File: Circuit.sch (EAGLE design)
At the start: 3 parts

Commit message: Added all the sensor components
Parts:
- added ITG1, ITG2, ITG3: ITG-3050, Gyros:ITG-3050
- added MPU1: MPU-3300, Gyros:MPU-3300
- added U1, U2: MAG3110, Gyros:MAG3110
- added U10, U7, U8, U9: MMA8452Q, SparkFun:MMA8452Q
- added U3, U4, U5, U6: L3G4200D, Gyros:L3G4200D
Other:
- moved on the sheet: ITG, MPU, U$1
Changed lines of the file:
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@@
 <part name="U$1" library="RaspberryPi" deviceset="RASPBERRY-PI_REV2" device=""/>
 <part name="ITG" library="Gyros" deviceset="ITG-3050" device=""/>
+<part name="MPU1" library="Gyros" deviceset="MPU-3300" device=""/>
+<part name="ITG1" library="Gyros" deviceset="ITG-3050" device=""/>
+<part name="ITG2" library="Gyros" deviceset="ITG-3050" device=""/>
+<part name="ITG3" library="Gyros" deviceset="ITG-3050" device=""/>
+<part name="U1" library="Gyros" deviceset="MAG3110" device=""/>
+<part name="U2" library="Gyros" deviceset="MAG3110" device=""/>
+<part name="U3" library="Gyros" deviceset="L3G4200D" device=""/>
+<part name="U4" library="Gyros" deviceset="L3G4200D" device=""/>
+<part name="U5" library="Gyros" deviceset="L3G4200D" device=""/>
+<part name="U6" library="Gyros" deviceset="L3G4200D" device=""/>
+<part name="U7" library="SparkFun" deviceset="MMA8452Q" device=""/>
+<part name="U8" library="SparkFun" deviceset="MMA8452Q" device=""/>
+<part name="U9" library="SparkFun" deviceset="MMA8452Q" device=""/>
+<part name="U10" library="SparkFun" deviceset="MMA8452Q" device=""/>
 </parts>
 <sheets>
@@
 </plain>
 <instances>
-<instance part="MPU" gate="G$1" x="124.06" y="71.68"/>
-<instance part="U$1" gate="G$1" x="181.58" y="-34.48"/>
-<instance part="ITG" gate="G$1" x="246.38" y="71.12"/>
+<instance part="MPU" gate="G$1" x="103.74" y="147.88"/>
+<instance part="U$1" gate="G$1" x="415.26" y="-31.94"/>
+<instance part="ITG" gate="G$1" x="246.38" y="86.36"/>
+<instance part="MPU1" gate="G$1" x="245.98" y="147.88"/>
+<instance part="ITG1" gate="G$1" x="104.14" y="86.36"/>
+<instance part="ITG2" gate="G$1" x="104.14" y="43.18"/>
+<instance part="ITG3" gate="G$1" x="246.38" y="43.18"/>
+<instance part="U1" gate="G$1" x="104.14" y="-111.76"/>
+<instance part="U2" gate="G$1" x="246.38" y="-111.76"/>
+<instance part="U3" gate="G$1" x="246.38" y="-20.32"/>
+<instance part="U4" gate="G$1" x="104.14" y="-20.32"/>
+<instance part="U5" gate="G$1" x="104.14" y="-66.04"/>
+<instance part="U6" gate="G$1" x="246.38" y="-66.04"/>
+<instance part="U7" gate="G$1" x="383.54" y="134.62"/>
+<instance part="U8" gate="G$1" x="454.66" y="134.62"/>
+<instance part="U9" gate="G$1" x="383.54" y="91.44"/>
+<instance part="U10" gate="G$1" x="454.66" y="91.44"/>
 </instances>
 <busses>

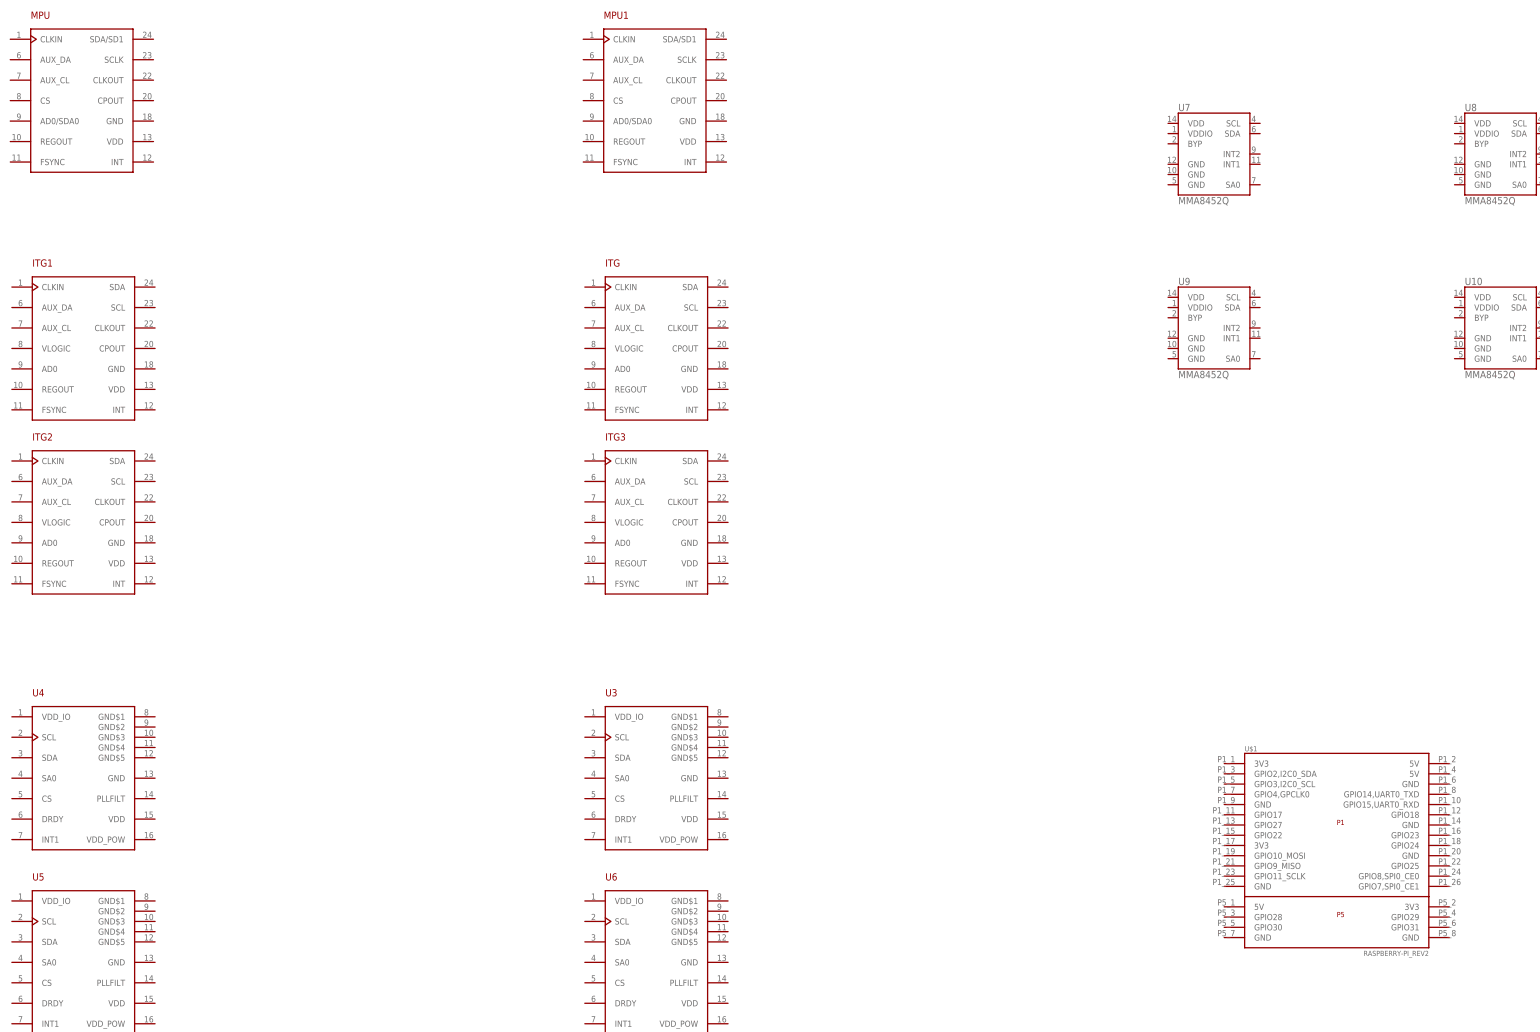
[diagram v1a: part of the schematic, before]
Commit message: Adds first routes
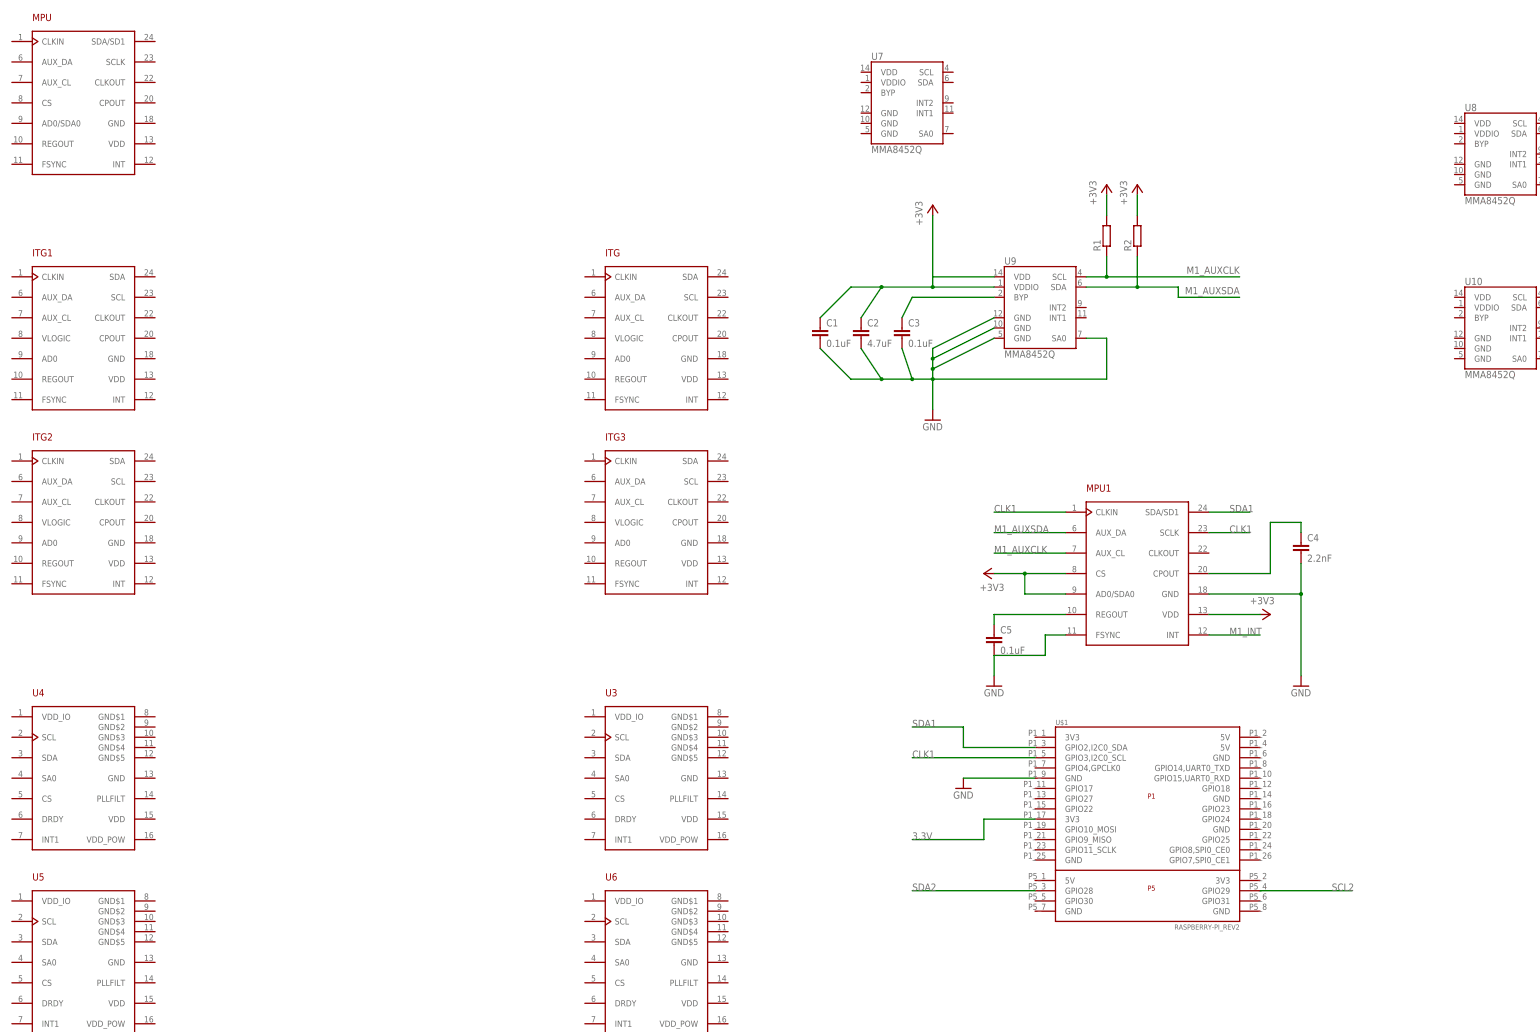
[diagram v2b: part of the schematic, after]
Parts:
- added C1, C3, C5: 0.1uF, SparkFun:CAP0402-CAP
- added C2: 4.7uF, SparkFun:CAP0402-CAP
- added C4: 2.2nF, SparkFun:CAP0402-CAP
- added R1, R2: (no value), resistor:R-EU_0207/10
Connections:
- new net +3V3: C1.1, C2.1, MPU1.AD0/SDA0, MPU1.CS, MPU1.VDD, R1.2, R2.2, U9.VDD, U9.VDDIO
- new net 3.3V: U$1.3V3@17
- new net CLK1: MPU1.CLKIN, MPU1.SCLK, U$1.GPIO3,I2C0_SCL
- new net GND: C1.2, C2.2, C3.2, C4.2, C5.2, MPU1.FSYNC, MPU1.GND, U$1.GND@9, U9.GND@0, U9.GND@1, U9.GND@2, U9.SA0
- new net M1_AUXCLK: MPU1.AUX_CL, R1.1, U9.SCL
- new net M1_AUXSDA: MPU1.AUX_DA, R2.1, U9.SDA
- new net M1_INT: MPU1.INT
- new net N$1: C4.1, MPU1.CPOUT
- new net N$2: C5.1, MPU1.REGOUT
- new net N$3: C3.1, U9.BYP
- new net SCL2: U$1.GPIO29
- new net SDA1: MPU1.SDA/SD1, U$1.GPIO2,I2C0_SDA
- new net SDA2: U$1.GPIO28
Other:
- moved on the sheet: ITG, ITG1, MPU, MPU1, U$1, U7, U9

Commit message: Added 4 itg setups
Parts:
- removed ITG: ITG-3050, Gyros:ITG-3050
- removed MPU: MPU-3300, Gyros:MPU-3300
- added C10, C11, C13, C14, C16, C18, C20, C21, C23, C25, C27, C28, C30, C32, C34, C35, C37, C6, C8: 0.1uF, SparkFun:CAP0402-CAP
- added C12, C19, C26, C33, C7: 4.7uF, SparkFun:CAP0402-CAP
- added C15, C22, C29, C36, C9: 2.2nF, SparkFun:CAP0402-CAP
- added C17, C24, C31, C38: 10nF, SparkFun:CAP0402-CAP
- added ITG4: ITG-3050, Gyros:ITG-3050
- added MPU2: MPU-3300, Gyros:MPU-3300
- added R10, R11, R12, R3, R4, R5, R6, R7, R8, R9: 10K, resistor:R-EU_0207/10
- added U11, U12: MMA8452Q, SparkFun:MMA8452Q
- R1, R2: value (none) -> 10K
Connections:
- removed net 3.3V: U$1.3V3@17
- removed net M1_INT: MPU1.INT
- new net CLK2: ITG2.SCL, ITG4.SCL, MPU2.SCLK
- new net I1_AUXCLK: ITG1.AUX_CL, U7.SCL
- new net I1_AUXSDA: ITG1.AUX_DA, U7.SDA
- new net I1_INT: ITG1.INT
- new net I2_AUXCLK: ITG2.AUX_CL, U8.SCL
- new net I2_AUXSDA: ITG2.AUX_DA, U8.SDA
- new net I2_INT: ITG2.INT
- new net I3_AUXCLK: ITG3.AUX_CL, U10.SCL
- new net I3_AUXSDA: ITG3.AUX_DA, U10.SDA
- new net I3_INT: ITG3.INT
- new net I4_AUXCLK: ITG4.AUX_CL, U12.SCL
- new net I4_AUXSDA: ITG4.AUX_DA, U12.SDA
- new net I4_INT: ITG4.INT
- new net M2_AUXCLK: MPU2.AUX_CL, R3.1, U11.SCL
- new net M2_AUXSDA: MPU2.AUX_DA, R4.1, U11.SDA
- new net M2_INT: MPU1.INT, MPU2.INT
- new net N$11: R5.1
- new net N$12: R6.1
- new net N$13: C14.1, ITG1.REGOUT
- new net N$14: C15.1, ITG1.CPOUT
- new net N$15: C20.1, U8.BYP
- new net N$18: R7.1
- new net N$19: R8.1
- new net N$20: C21.1, ITG2.REGOUT
- new net N$21: C22.1, ITG2.CPOUT
- new net N$23: C27.1, U10.BYP
- new net N$25: R9.1
- new net N$26: R10.1
- new net N$27: C28.1, ITG3.REGOUT
- new net N$28: C29.1, ITG3.CPOUT
- new net N$30: C34.1, U12.BYP
- new net N$32: R11.1
- new net N$33: R12.1
- new net N$34: C35.1, ITG4.REGOUT
- new net N$35: C36.1, ITG4.CPOUT
- new net N$5: C8.1, U11.BYP
- new net N$6: C9.1, MPU2.CPOUT
- new net N$7: C10.1, MPU2.REGOUT
- new net N$9: C13.1, U7.BYP
- net +3V3: now also C11.1, C12.1, C15.2, C16.1, C16.2, C17.1, C18.1, C19.1, C22.2, C23.1, C23.2, C24.1, C25.1, C26.1, C29.2, C30.1, C30.2, C31.1, C32.1, C33.1, C36.2, C37.1, C37.2, C38.1, C6.1, C7.1, ITG1.GND, ITG1.VDD, ITG1.VLOGIC, ITG2.GND, ITG2.VDD, ITG2.VLOGIC, ITG3.GND, ITG3.VDD, ITG3.VLOGIC, ITG4.GND, ITG4.VDD, ITG4.VLOGIC, MPU2.CS, MPU2.VDD, R10.2, R11.2, R12.2, R3.2, R4.2, R5.2, R6.2, R7.2, R8.2, R9.2, U$1.3V3@17, U10.VDD, U10.VDDIO, U11.VDD, U11.VDDIO, U12.VDD, U12.VDDIO, U7.VDD, U7.VDDIO, U8.VDD, U8.VDDIO
- net CLK1: now also ITG1.SCL, ITG3.SCL; no longer MPU1.CLKIN
- net GND: now also C10.2, C11.2, C12.2, C13.2, C14.2, C17.2, C18.2, C19.2, C20.2, C21.2, C24.2, C25.2, C26.2, C27.2, C28.2, C31.2, C32.2, C33.2, C34.2, C35.2, C38.2, C6.2, C7.2, C8.2, C9.2, ITG1.CLKIN, ITG1.FSYNC, ITG2.CLKIN, ITG2.FSYNC, ITG3.CLKIN, ITG3.FSYNC, ITG4.CLKIN, ITG4.FSYNC, MPU1.CLKIN, MPU2.AD0/SDA0, MPU2.CLKIN, MPU2.FSYNC, MPU2.GND, U10.GND@0, U10.GND@1, U10.GND@2, U10.SA0, U11.GND@0, U11.GND@1, U11.GND@2, U11.SA0, U12.GND@0, U12.GND@1, U12.GND@2, U12.SA0, U7.GND@0, U7.GND@1, U7.GND@2, U7.SA0, U8.GND@0, U8.GND@1, U8.GND@2, U8.SA0
- net SDA1: now also ITG1.SDA, ITG3.SDA
- net SDA2: now also ITG2.SDA, ITG4.SDA, MPU2.SDA/SD1
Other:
- note added: "MPU/MMA_1"
- note added: "MPU/MMA_2"
- moved on the sheet: C1, C2, C3, C4, C5, ITG1, ITG2, ITG3, MPU1, R1, R2, U$1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

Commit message: Added L3G4 gyros
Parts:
- added C39, C43, C47, C51: 0.1uF, SparkFun:CAP0402-CAP
- added C40, C44, C48, C52: 10uF, SparkFun:CAP0402-CAP
- added C41, C45, C49, C53: 10nF, SparkFun:CAP0402-CAP
- added C42, C46, C50, C54: 470nF, SparkFun:CAP0402-CAP
- added R13, R14, R15, R16, R17, R18, R19, R20, R21, R22, R23, R24: 10K, resistor:R-EU_0207/10
- U3, U4, U5, U6: device Gyros:L3G4200D -> SparkFun:L3G4200D
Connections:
- new net N$36: C45.1, C46.1, U4.PLL
- new net N$39: C41.1, C42.1, U3.PLL
- new net N$40: C42.2, R15.2
- new net N$41: C46.2, R18.2
- new net N$45: C49.1, C50.1, U5.PLL
- new net N$46: C50.2, R21.2
- new net N$50: C53.1, C54.1, U6.PLL
- new net N$51: C54.2, R24.2
- net +3V3: now also C39.1, C40.1, C43.1, C44.1, C47.1, C48.1, C51.1, C52.1, R13.1, R14.1, R16.1, R17.1, R19.1, R20.1, R22.1, R23.1, U3.CS, U3.RSVDV@0, U3.VDD, U3.VDDIO, U4.CS, U4.RSVDV@0, U4.SDO, U4.VDD, U4.VDDIO, U5.CS, U5.RSVDV@0, U5.VDD, U5.VDDIO, U6.CS, U6.RSVDV@0, U6.SDO, U6.VDD, U6.VDDIO
- net CLK1: now also R13.2, R16.2, U3.SCL, U4.SCL
- net CLK2: now also R19.2, R22.2, U5.SCL, U6.SCL
- net GND: now also C39.2, C40.2, C41.2, C43.2, C44.2, C45.2, C47.2, C48.2, C49.2, C51.2, C52.2, C53.2, R15.1, R18.1, R21.1, R24.1, U3.GND, U3.RSDVG@3, U3.RSVDG@0, U3.RSVDG@1, U3.RSVDG@2, U3.RSVDG@4, U3.SDO, U4.GND, U4.RSDVG@3, U4.RSVDG@0, U4.RSVDG@1, U4.RSVDG@2, U4.RSVDG@4, U5.GND, U5.RSDVG@3, U5.RSVDG@0, U5.RSVDG@1, U5.RSVDG@2, U5.RSVDG@4, U5.SDO, U6.GND, U6.RSDVG@3, U6.RSVDG@0, U6.RSVDG@1, U6.RSVDG@2, U6.RSVDG@4
- net SDA1: now also R14.2, R17.2, U3.SDA/SDI, U4.SDA/SDI
- net SDA2: now also R20.2, R23.2, U5.SDA/SDI, U6.SDA/SDI
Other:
- moved on the sheet: U$1, U1, U2

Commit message: Added mags and box labels
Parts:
- added C55, C56, C57, C58: 0.1uF, SparkFun:CAP0402-CAP
- added R25, R26, R27, R28: 4.7K, resistor:R-EU_0207/10
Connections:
- new net MAG1_INT: U1.INT1
- new net MAG2_INT: U2.INT1
- new net N$38: C55.1, U2.CAP-A
- new net N$49: C56.1, U2.CAP-R
- new net N$52: C57.1, U1.CAP-A
- new net N$53: C58.1, U1.CAP-R
- net +3V3: now also R25.2, R26.2, R27.2, R28.2, U1.VDD, U1.VDDIO, U2.VDD, U2.VDDIO
- net CLK1: now also R28.1, U1.SCL
- net CLK2: now also R26.1, U2.SCL
- net GND: now also C55.2, C56.2, C57.2, C58.2, U1.GND@10, U1.GND@5, U2.GND@10, U2.GND@5
- net SDA1: now also R27.1, U1.SDA
- net SDA2: now also R25.1, U2.SDA
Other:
- moved on the sheet: U1, U2

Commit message: Organised the board layout, requires autorouting
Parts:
- added R29, R30: 10K, resistor:R-EU_0207/10
- added U$2, U$3: PCA9546A, Gyros:PCA9546A
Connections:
- new net B1_SC0: ITG1.SCL, MPU1.SCLK, U$2.SC0
- new net B1_SC1: ITG3.SCL, R13.2, U$2.SC1, U3.SCL
- new net B1_SC2: R28.1, U$2.SC2, U1.SCL, U4.SCL
- new net B1_SD0: ITG1.SDA, MPU1.SDA/SD1, U$2.SD0
- new net B1_SD1: ITG3.SDA, R14.2, U$2.SD1, U3.SDA/SDI
- new net B1_SD2: R27.1, U$2.SD2, U1.SDA, U4.SDA/SDI
- new net B2_SC0: ITG2.SCL, MPU2.SCLK, U$3.SC0
- new net B2_SC1: ITG4.SCL, R19.2, U$3.SC1, U5.SCL
- new net B2_SC2: R22.2, R26.1, U$3.SC2, U2.SCL, U6.SCL
- new net B2_SD0: ITG2.SDA, MPU2.SDA/SD1, U$3.SD0
- new net B2_SD1: ITG4.SDA, R20.2, U$3.SD1, U5.SDA/SDI
- new net B2_SD2: R23.2, R25.1, U$3.SD2, U2.SDA, U6.SDA/SDI
- new net N$16: R30.2, U$3.RESET
- new net N$42: R29.2, U$2.RESET
- net +3V3: now also ITG3.AD0, ITG4.AD0, MPU2.AD0/SDA0, R29.1, R30.1, U$2.A2, U$2.VCC, U$3.A2, U$3.VCC
- net CLK1: now also U$2.SCL; no longer ITG1.SCL, ITG3.SCL, MPU1.SCLK, R13.2, R28.1, U1.SCL, U3.SCL, U4.SCL
- net CLK2: now also U$3.SCL; no longer ITG2.SCL, ITG4.SCL, MPU2.SCLK, R19.2, R22.2, R26.1, U2.SCL, U5.SCL, U6.SCL
- net GND: now also ITG1.AD0, ITG2.AD0, U$2.A0, U$2.A1, U$2.GND, U$3.A0, U$3.A1, U$3.GND; no longer MPU2.AD0/SDA0
- net SDA1: now also U$2.SDA; no longer ITG1.SDA, ITG3.SDA, MPU1.SDA/SD1, R14.2, R27.1, U1.SDA, U3.SDA/SDI, U4.SDA/SDI
- net SDA2: now also U$3.SDA; no longer ITG2.SDA, ITG4.SDA, MPU2.SDA/SD1, R20.2, R23.2, R25.1, U2.SDA, U5.SDA/SDI, U6.SDA/SDI
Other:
- note added: "0x0E"
- note added: "0x68"
- note added: "0x69"
- moved on the sheet: C1, C10, C11, C12, C13, C14, C15, C16, C17, C18, C19, C2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

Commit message: Rearranged as per phil
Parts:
- added IC1: LM1117T-3.3-V, Gyros:LM1117T-3.3-V
- added R31, R32, R33, R34, R35, R36, R37, R38, R39, R40: 2.2K, resistor:R-EU_0207/10
- R1, R10, R11, R12, R13, R14, R16, R17, R19, R2, R20, R22, R23, R3, R4, R5, R6, R7, R8, R9: value 10K -> 2.2K
- R25, R26, R27, R28: value 4.7K -> 2.2K
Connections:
- new net N$10: IC1.IN, U$1.5V@2
- new net N$17: IC1.GND, U$1.GND@14
- net +3V3: now also IC1.OUT, R31.1, R32.1, R33.2, R34.2, R35.1, R36.1, R37.1, R38.1, R39.1, R40.1; no longer U$1.3V3@17
- net B1_SC0: now also R32.2
- net B1_SC1: now also R38.2
- net B1_SD0: now also R31.2
- net B1_SD1: now also R37.2
- net B2_SC0: now also R36.2
- net B2_SC1: now also R40.2
- net B2_SD0: now also R35.2
- net B2_SD1: now also R39.2
- net SCL2: now also R34.1
- net SDA2: now also R33.1
